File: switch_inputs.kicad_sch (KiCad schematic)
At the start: 20 parts, among them U1 PRTR5V0U2X, U2 PRTR5V0U2X, U3 PRTR5V0U2X, U4 PRTR5V0U2X

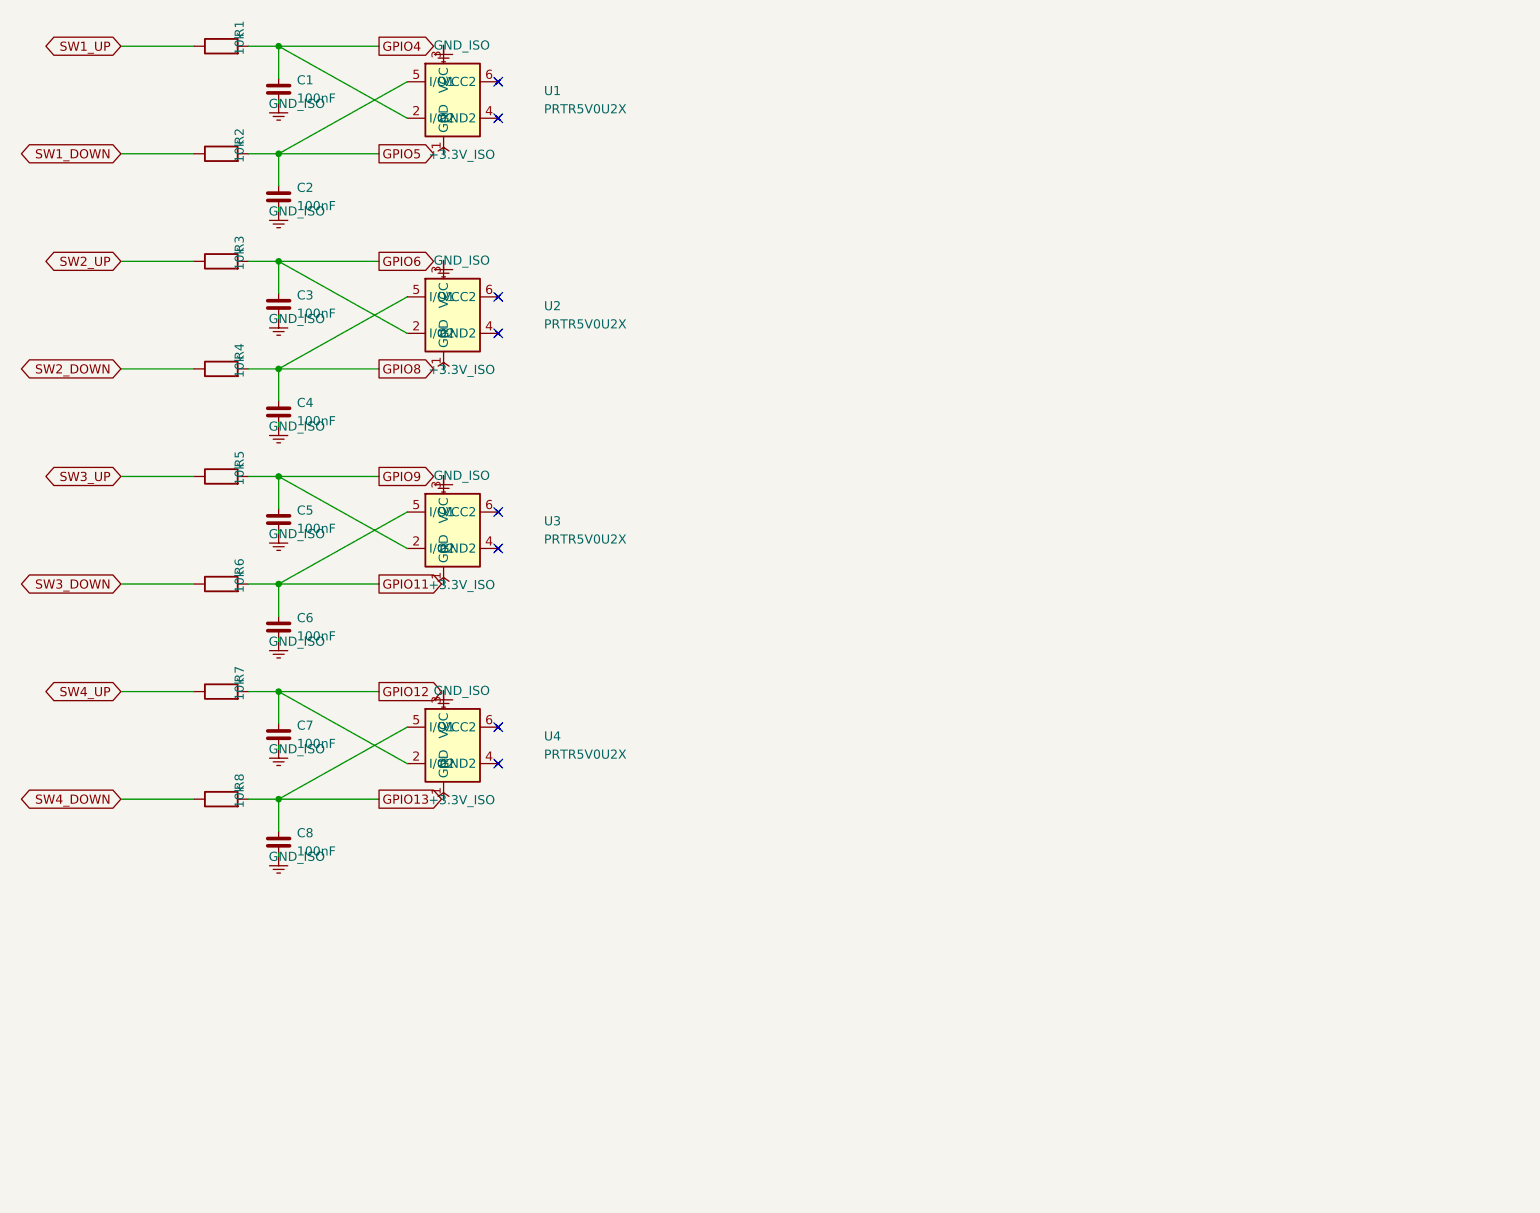
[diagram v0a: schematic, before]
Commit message: Updated USB to switch from USB-C to Micro
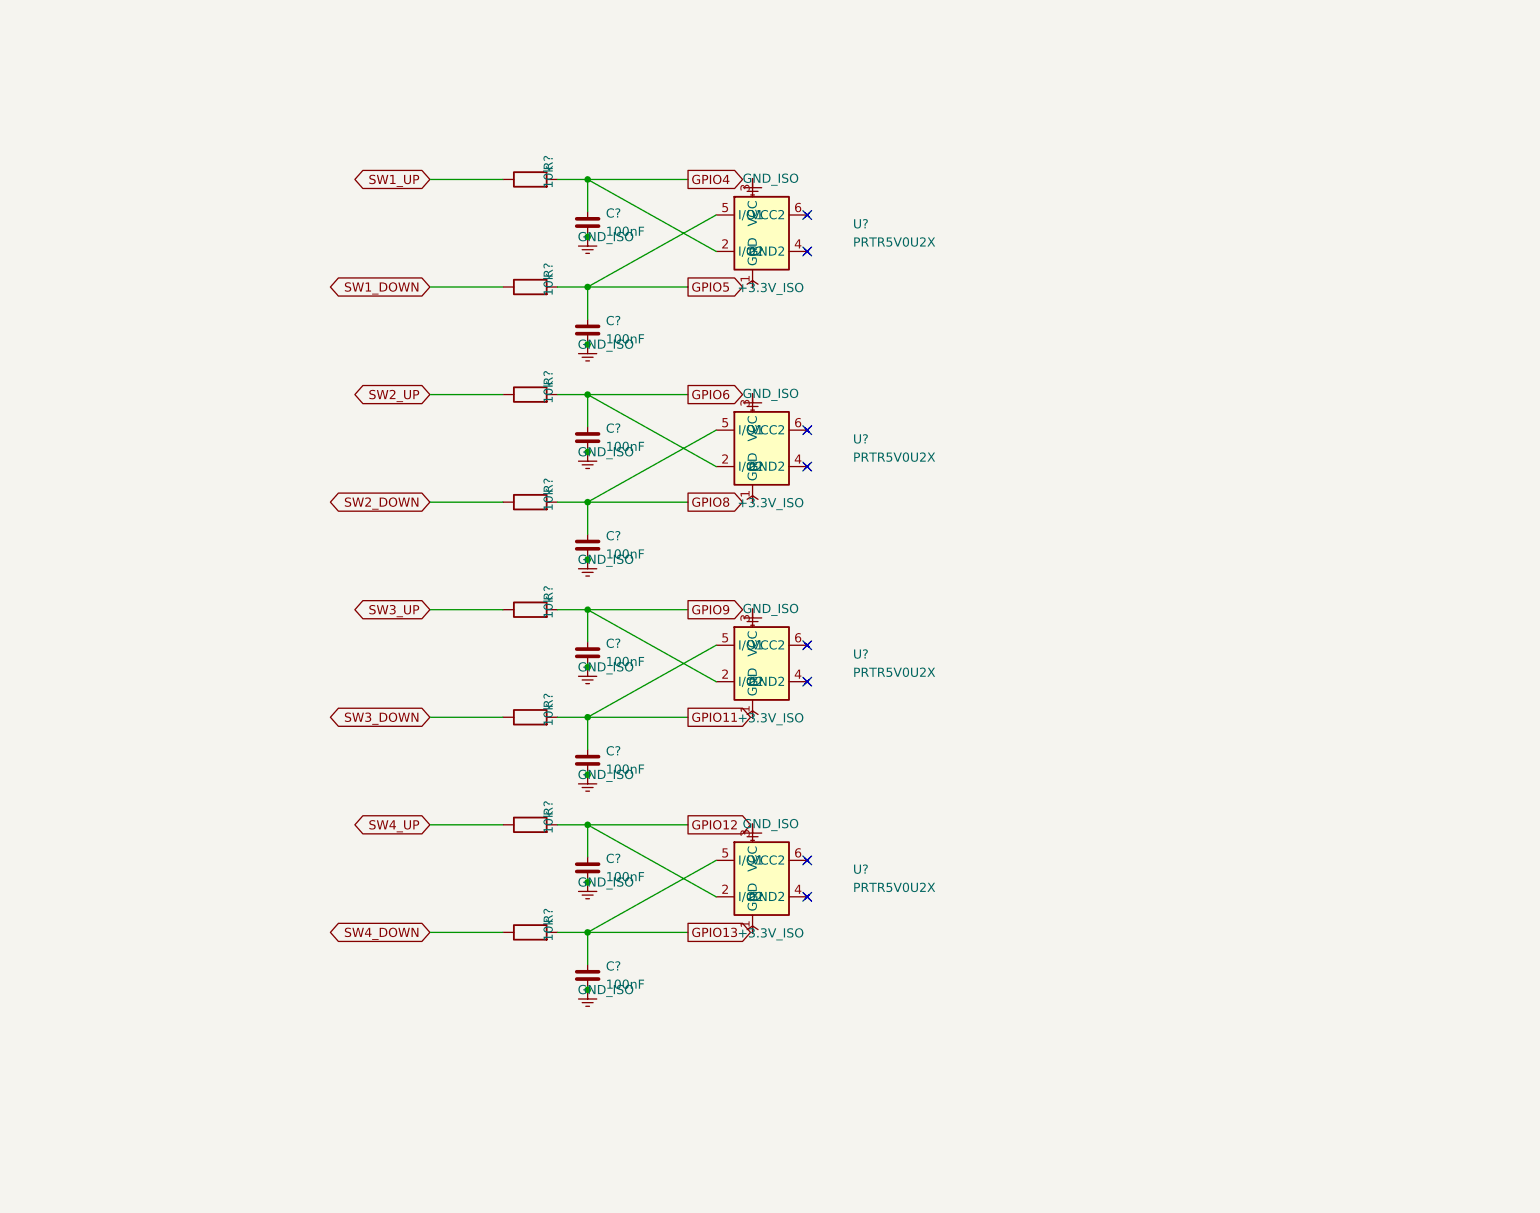
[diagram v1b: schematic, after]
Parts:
- renumbered C8 to C?, C2 to C?, C6 to C?, C5 to C?, C1 to C?, C3 to C?, C7 to C?, C4 to C?, R4 to R?, R3 to R?, R8 to R?, R5 to R?, R1 to R?, R7 to R?, R6 to R?, R2 to R?, U4 to U?, U3 to U?, U1 to U?, U2 to U?
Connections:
- net GND_ISO: now also C?.2, C?.2, C?.2, C?.2, C?.2, C?.2, C?.2, C?.2
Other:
- moved on the sheet: C?, R?, U?

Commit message: Updating routing with new terminal block
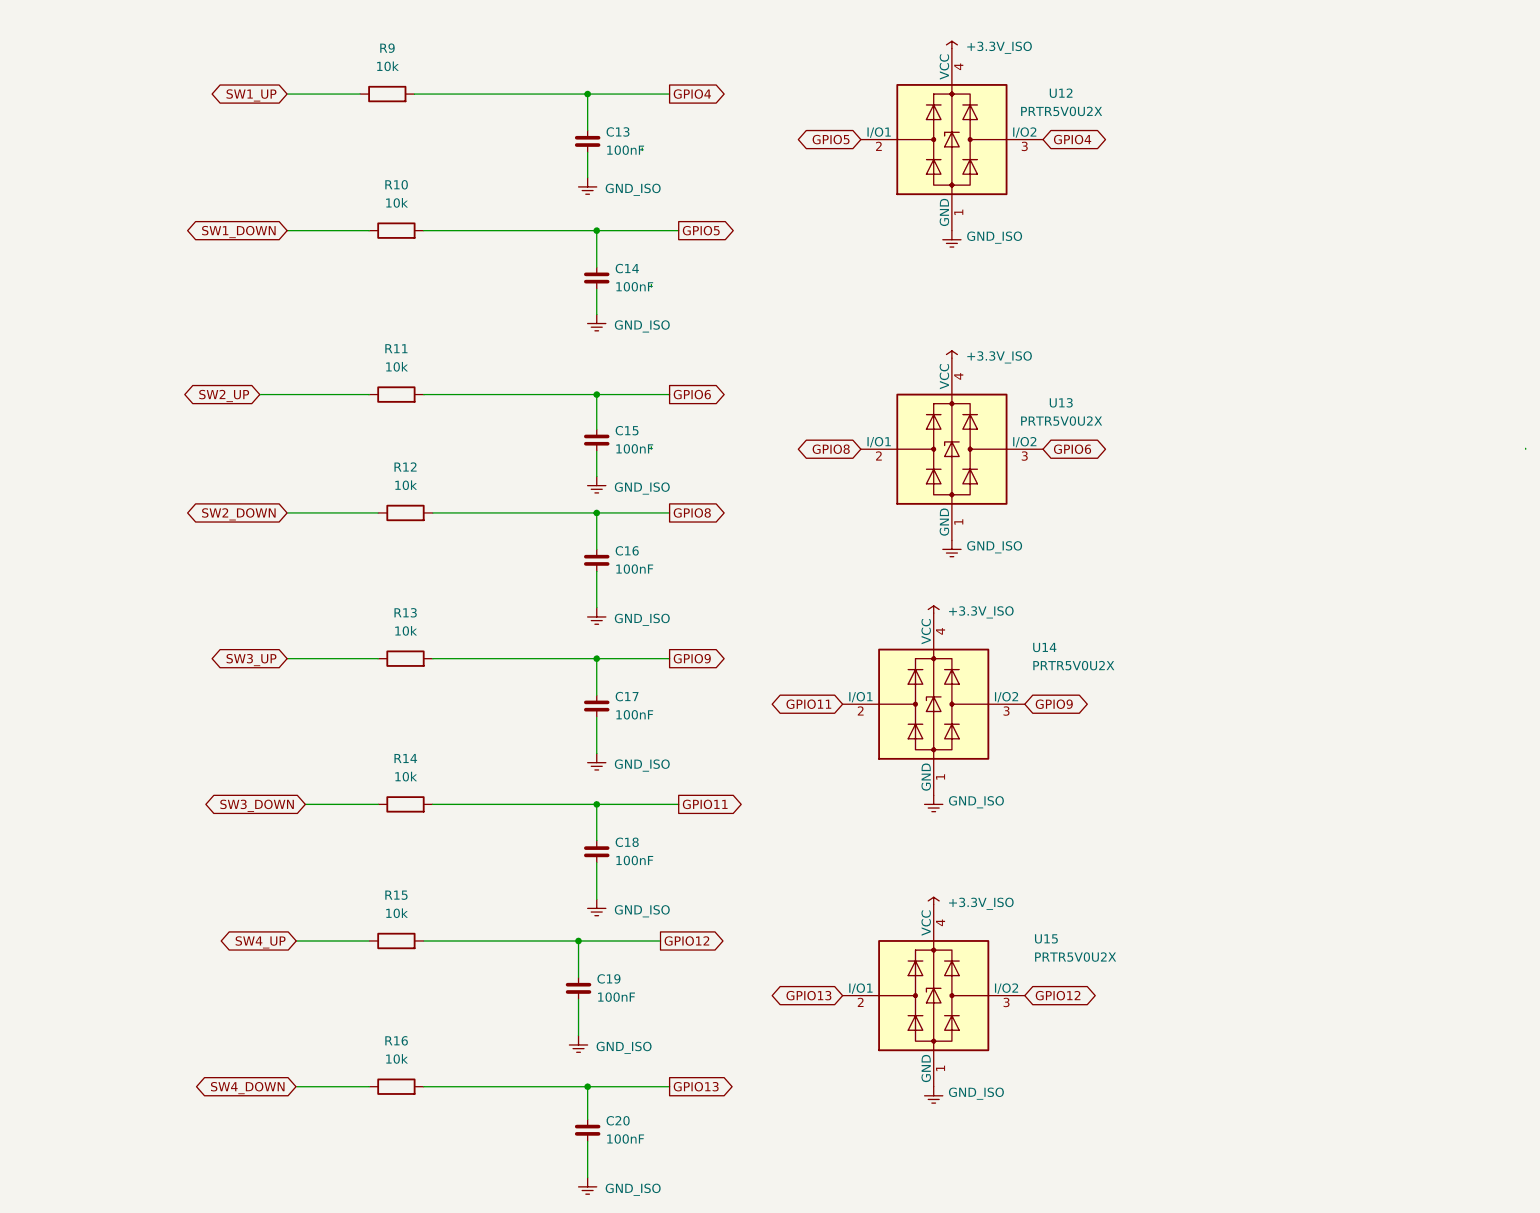
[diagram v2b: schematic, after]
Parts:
- removed C? (x7): 100nF, Capacitor_SMD:C_0402_1005Metric, symbol Device:C
- removed R? (x8): 10k, Resistor_SMD:R_0402_1005Metric, symbol Device:R
- removed U? (x4): PRTR5V0U2X, Package_TO_SOT_SMD:SOT-363, symbol PRTR5V0U2X
- added C13, C14, C15, C16, C17, C18, C19: 100nF, Capacitor_SMD:C_0402_1005Metric, symbol Device:C
- added R10, R11, R12, R13, R14, R15, R9: 10k, Resistor_SMD:R_0603_1608Metric, symbol Device:R
- added R16: 10k, Diode_SMD:D_0805_2012Metric, symbol Device:R
- added U12, U13, U14, U15: PRTR5V0U2X, Package_TO_SOT_SMD:SOT-143, symbol Power_Protection:PRTR5V0U2X
- gave numbers to parts that had none: 1
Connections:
- net +3.3V_ISO: now also U12.4 (VCC), U13.4 (VCC), U14.4 (VCC), U15.4 (VCC)
- net GND_ISO: now also C13.2, C14.2, C15.2, C16.2, C17.2, C18.2, C19.2, U12.1 (GND), U13.1 (GND), U14.1 (GND), U15.1 (GND)
- net GPIO11: now also C18.1, R14.2, U14.2 (I/O1)
- net GPIO12: now also C19.1, R15.2, U15.3 (I/O2)
- net GPIO13: now also R16.2, U15.2 (I/O1)
- net GPIO4: now also C13.1, R9.2, U12.3 (I/O2)
- net GPIO5: now also C14.1, R10.2, U12.2 (I/O1)
- net GPIO6: now also C15.1, R11.2, U13.3 (I/O2)
- net GPIO8: now also C16.1, R12.2, U13.2 (I/O1)
- net GPIO9: now also C17.1, R13.2, U14.3 (I/O2)
- net SW1_DOWN: now also R10.1
- net SW1_UP: now also R9.1
- net SW2_DOWN: now also R12.1
- net SW2_UP: now also R11.1
- net SW3_DOWN: now also R14.1
- net SW3_UP: now also R13.1
- net SW4_DOWN: now also R16.1
- net SW4_UP: now also R15.1
- no-connect marks 8 -> 0
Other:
- moved on the sheet: C20

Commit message: Adding switches to PCB
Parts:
- R16: footprint Diode_SMD:D_0805_2012Metric -> Resistor_SMD:R_0603_1608Metric
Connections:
- net GPIO11 renamed SW3_DOWN_IN
- net GPIO12 renamed SW4_UP_IN
- net GPIO13 renamed SW4_DOWN_IN
- net GPIO4 renamed SW1_UP_IN
- net GPIO5 renamed SW1_DOWN_IN
- net GPIO6 renamed SW2_UP_IN
- net GPIO8 renamed SW2_DOWN_IN
- net GPIO9 renamed SW3_UP_IN
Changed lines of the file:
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@@
 		)
 	)
-	(global_label "GPIO12"
+	(global_label "SW4_UP_IN"
 		(shape output)
 		(at 95.25 144.78 0)
@@
 		)
 	)
-	(global_label "GPIO8"
+	(global_label "SW2_DOWN_IN"
 		(shape output)
 		(at 96.52 85.09 0)
@@
 		)
 	)
-	(global_label "GPIO11"
+	(global_label "SW3_DOWN_IN"
 		(shape bidirectional)
 		(at 120.65 111.76 180)
@@
 		)
 	)
-	(global_label "GPIO5"
+	(global_label "SW1_DOWN_IN"
 		(shape output)
 		(at 97.79 45.72 0)
@@
 		)
 	)
-	(global_label "GPIO9"
+	(global_label "SW3_UP_IN"
 		(shape bidirectional)
 		(at 146.05 111.76 0)
@@
 		)
 	)
-	(global_label "GPIO9"
+	(global_label "SW3_UP_IN"
 		(shape output)
 		(at 96.52 105.41 0)
@@
 		)
 	)
-	(global_label "GPIO13"
+	(global_label "SW4_DOWN_IN"
 		(shape bidirectional)
 		(at 120.65 152.4 180)
@@
 		)
 	)
-	(global_label "GPIO6"
+	(global_label "SW2_UP_IN"
 		(shape bidirectional)
 		(at 148.59 76.2 0)
@@
 		)
 	)
-	(global_label "GPIO4"
+	(global_label "SW1_UP_IN"
 		(shape output)
 		(at 96.52 26.67 0)
@@
 		)
 	)
-	(global_label "GPIO5"
+	(global_label "SW1_DOWN_IN"
 		(shape bidirectional)
 		(at 123.19 33.02 180)
@@
 		)
 	)
-	(global_label "GPIO12"
+	(global_label "SW4_UP_IN"
 		(shape bidirectional)
 		(at 146.05 152.4 0)
@@
 		)
 	)
-	(global_label "GPIO6"
+	(global_label "SW2_UP_IN"
 		(shape output)
 		(at 96.52 68.58 0)
@@
 		)
 	)
-	(global_label "GPIO11"
+	(global_label "SW3_DOWN_IN"
 		(shape output)
 		(at 97.79 125.73 0)
@@
 		)
 	)
-	(global_label "GPIO4"
+	(global_label "SW1_UP_IN"
 		(shape bidirectional)
 		(at 148.59 33.02 0)
@@
 		)
 	)
-	(global_label "GPIO8"
+	(global_label "SW2_DOWN_IN"
 		(shape bidirectional)
 		(at 123.19 76.2 180)
@@
 		)
 	)
-	(global_label "GPIO13"
+	(global_label "SW4_DOWN_IN"
 		(shape output)
 		(at 96.52 165.1 0)
@@
 			)
 		)
-		(property "Footprint" "Diode_SMD:D_0805_2012Metric"
+		(property "Footprint" "Resistor_SMD:R_0603_1608Metric"
 			(at 58.42 166.878 90)
 			(hide yes)

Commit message: Update annotations, fixed font sizes.
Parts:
- renumbered C13 to C1, C14 to C2, C15 to C3, C16 to C4, C17 to C5, C18 to C6, C19 to C7, C20 to C8, R9 to R1, R10 to R2, R11 to R3, R12 to R4, R13 to R5, R14 to R6, R15 to R7, R16 to R8
